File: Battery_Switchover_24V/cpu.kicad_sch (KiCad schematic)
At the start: 37 parts, among them J1 USB_C_Receptacle_USB2.0_14P, J7 Conn_01x05, SW1 SW_Push, U10 LPC11U67JBD48, U14 OPA2197xD

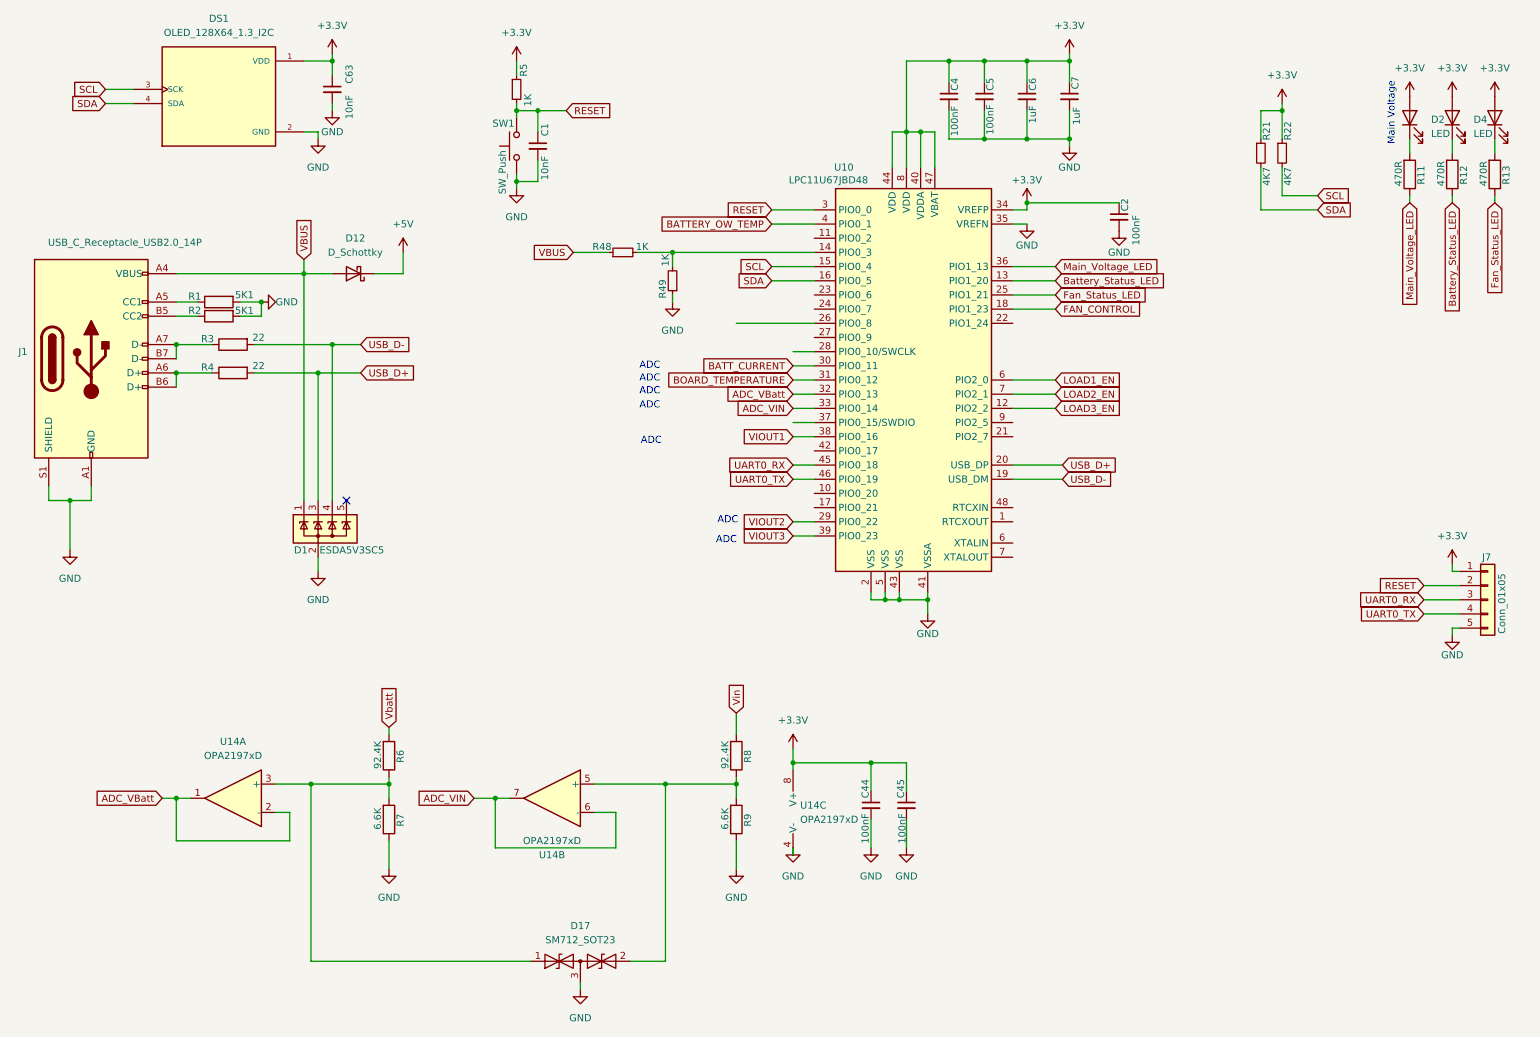
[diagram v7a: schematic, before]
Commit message: load switches positioned
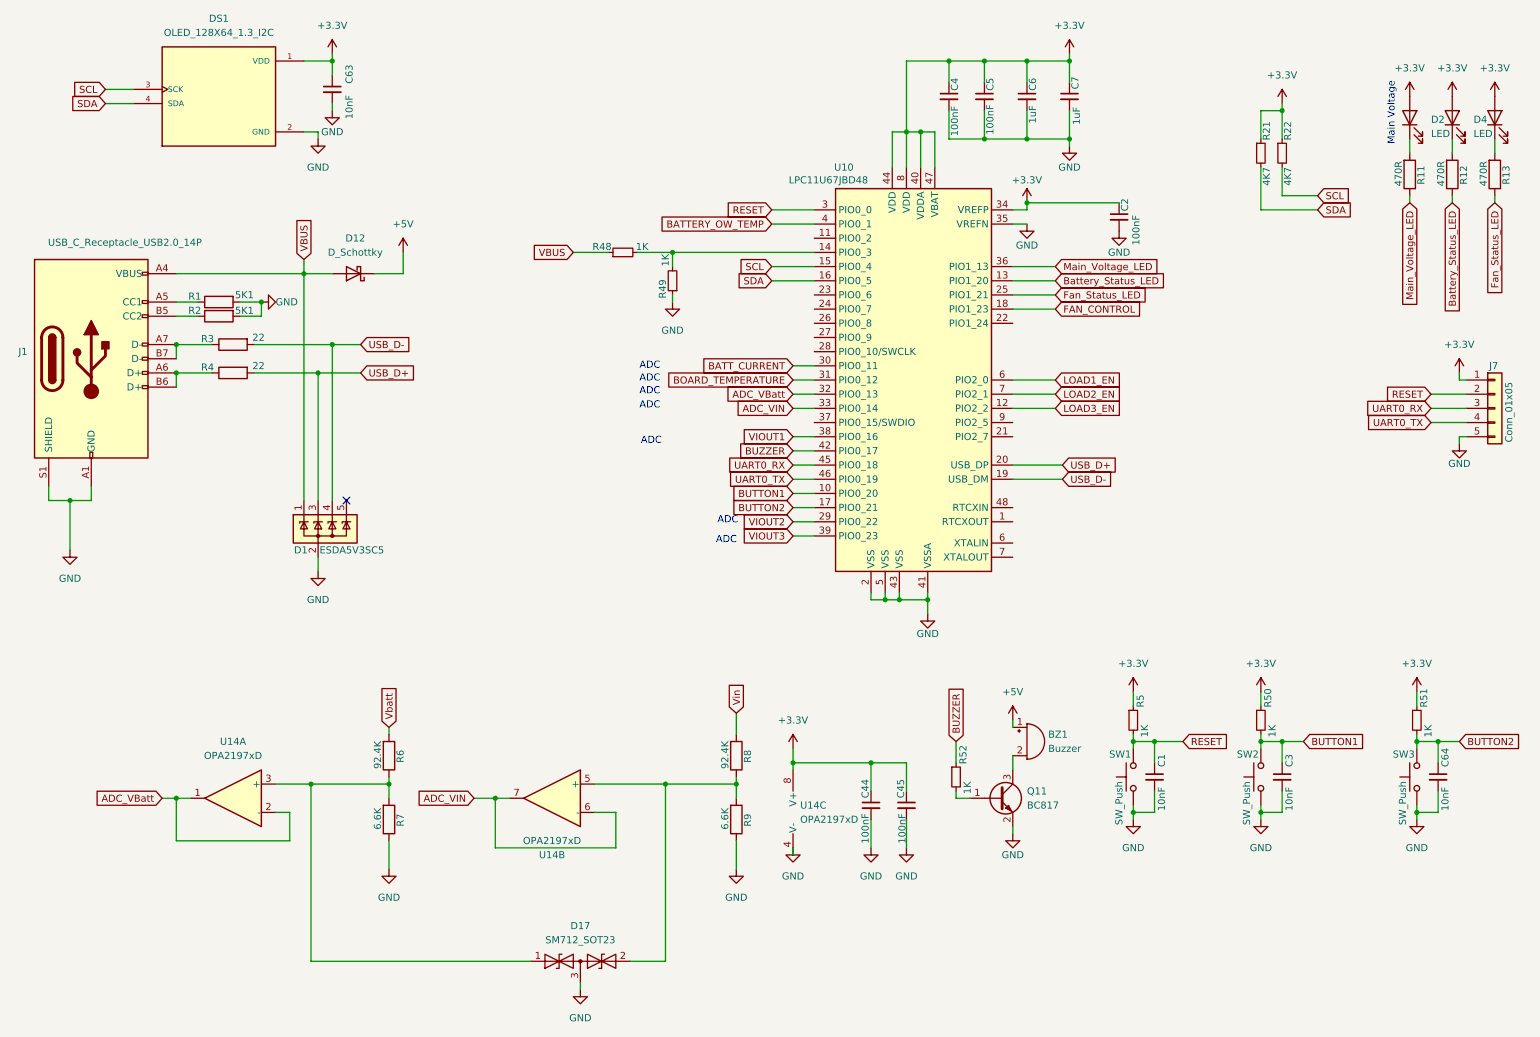
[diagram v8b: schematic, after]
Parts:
- added BZ1: Buzzer, Buzzer_Beeper:MagneticBuzzer_CUI_CMT-8504-100-SMT, symbol Device:Buzzer
- added C3, C64: 10nF, Capacitor_SMD:C_0603_1608Metric, symbol Device:C_Small
- added Q11: BC817, Package_TO_SOT_SMD:SOT-23, symbol Transistor_BJT:BC817
- added R50, R51, R52: 1K, Resistor_SMD:R_0603_1608Metric, symbol Device:R_Small
- added SW2, SW3: SW_Push, Button_Switch_SMD:SW_SPST_TL3305A, symbol changes:SW_Push
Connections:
- net +3.3V: now also R50.1, R51.1
- net +5V: now also BZ1.1 (+)
- net GND: now also C3.2, C64.2, Q11.2 (E), SW2.1, SW3.1
- net BUTTON1: now reaches U10.10 (PIO0_20)
- net BUTTON1: now also C3.1, R50.2, SW2.2
- net BUTTON2: now reaches U10.17 (PIO0_21)
- net BUTTON2: now also C64.1, R51.2, SW3.2
- net BUZZER: now reaches U10.42 (PIO0_17)
- net BUZZER: now also R52.1
- new net: Q11.1 (B), R52.2
- new net: BZ1.2 (-), Q11.3 (C)
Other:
- moved on the sheet: C1, J7, R5, SW1
